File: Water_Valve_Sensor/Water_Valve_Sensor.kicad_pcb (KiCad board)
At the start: 2 copper layers, 73.5 x 30 mm, 30 parts, among them J1 Barrel_Jack, J2 WATER_PROBE, J3 SENSITIVITY_SELECTOR, J5 VALVE, Q1 Q_PMOS_DGS, U1 NE555D, U2 LM2904, U3 47U

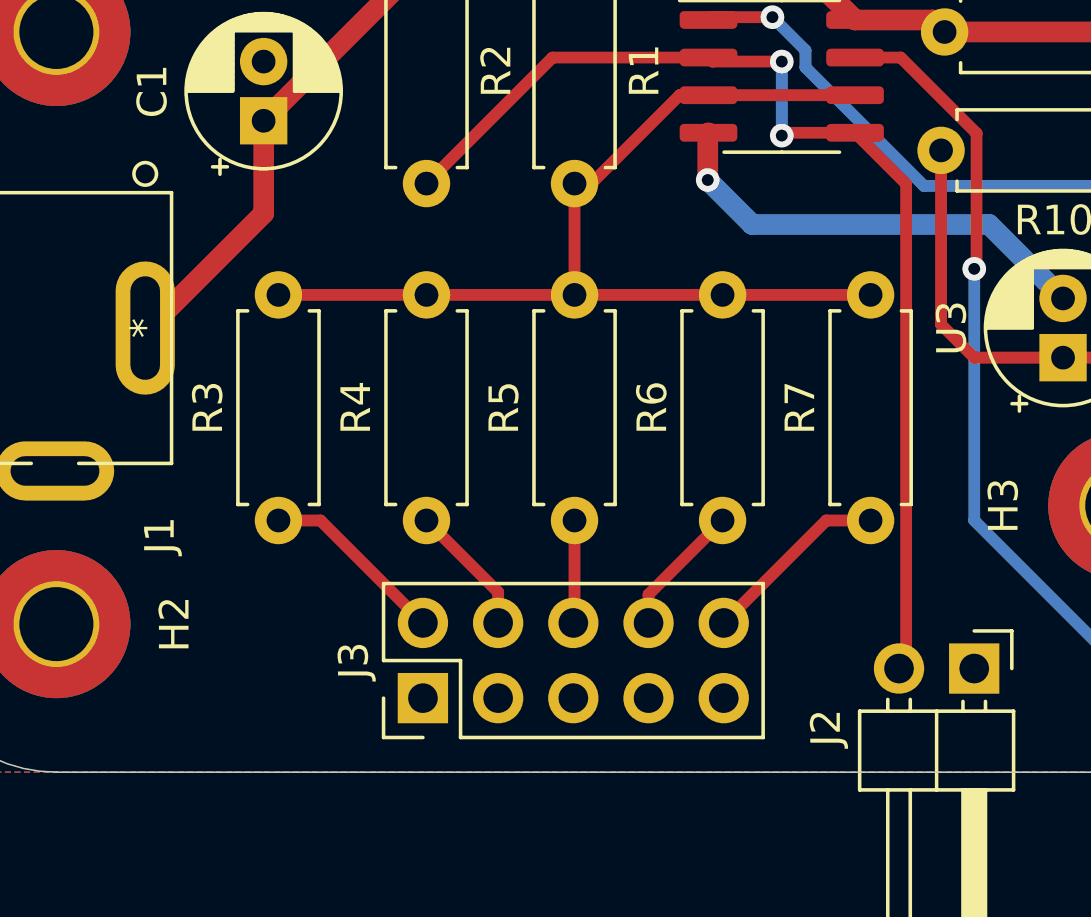
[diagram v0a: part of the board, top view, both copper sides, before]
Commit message: Fixed Wiring Issue
Added support for 2x6 header for Custom Setting Attachment
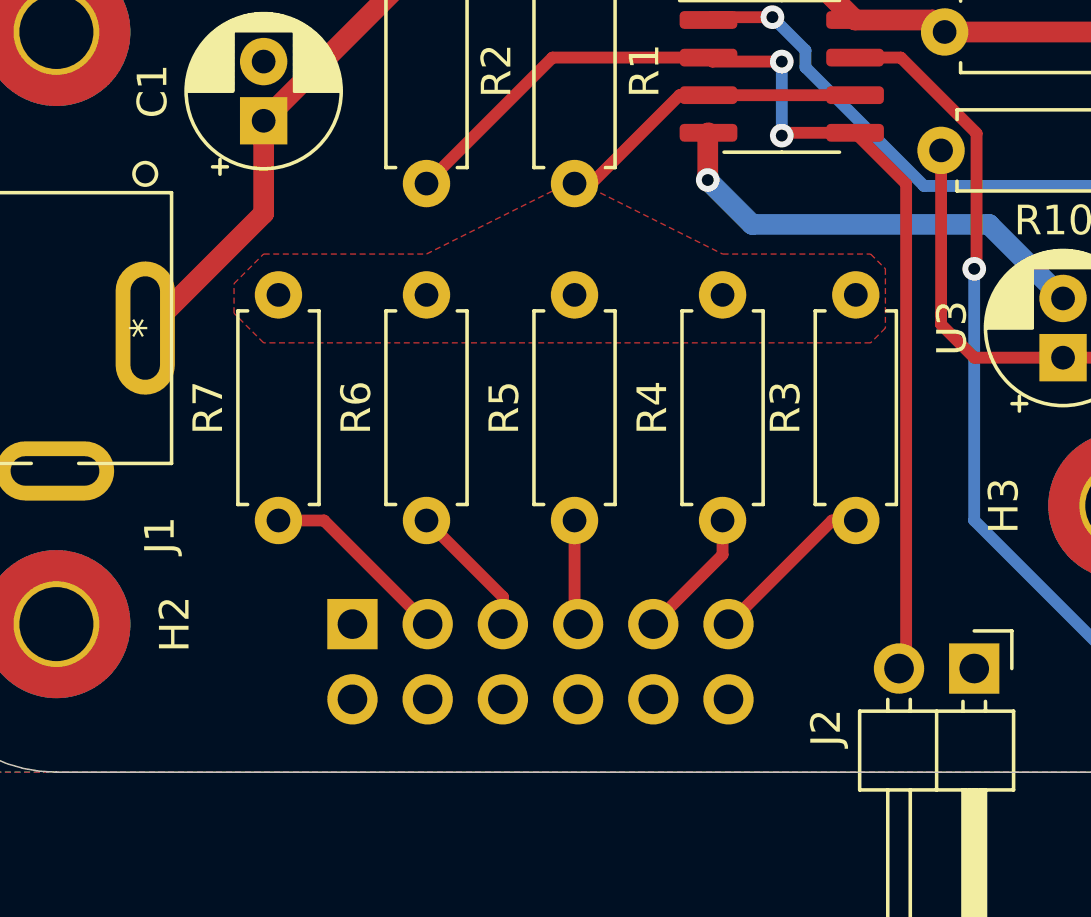
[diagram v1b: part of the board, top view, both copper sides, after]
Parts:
- J3: footprint Connector_PinHeader_2.54mm:PinHeader_2x05_P2.54mm_Vertical -> Connector_PinHeader_2.54mm:PinHeader_2x06_P2.54mm_Vertical; moved to B.Cu
- moved R7 20.0 mm to (47.5, 142.5)
- moved R3 19.5 mm to (67.0, 142.5)
- moved R4 10.0 mm to (62.5, 142.5)
- moved R6 10.0 mm to (52.5, 142.5)
- moved J3 3.45 mm to (50.0, 146.0), turned to 270 degrees
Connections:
- J3 pad 1: GND -> +12V
- J3 pad 10: Net-(J3-Pad10) -> GND
- J3 pad 2: Net-(J3-Pad2) -> +12V
- J3 pad 3: GND -> Net-(J3-Pad3)
- J3 pad 4: Net-(J3-Pad4) -> GND
- J3 pad 5: GND -> Net-(J3-Pad5)
- J3 pad 6: Net-(J3-Pad6) -> GND
- J3 pad 7: GND -> Net-(J3-Pad7)
- J3 pad 8: Net-(J3-Pad8) -> GND
- J3 pad 9: GND -> Net-(J3-Pad9)
- R3 pad 1: Net-(J3-Pad2) -> Net-(J3-Pad11)
- R4 pad 1: Net-(J3-Pad4) -> Net-(J3-Pad9)
- R5 pad 1: Net-(J3-Pad6) -> Net-(J3-Pad7)
- R6 pad 1: Net-(J3-Pad8) -> Net-(J3-Pad5)
- R7 pad 1: Net-(J3-Pad10) -> Net-(J3-Pad3)
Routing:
- net R_SENSITIVITY: track 34.5 -> 10.7 mm
- net Net-(J3-Pad3): track 0.00 -> 6.49 mm
- net Net-(J3-Pad10): track 6.39 -> 0.00 mm
- net Net-(J3-Pad2): track 6.31 -> 0.00 mm
- net Net-(J3-Pad11): track 0.00 -> 5.75 mm
- net Net-(J3-Pad5): track 0.00 -> 4.57 mm
- net Net-(J3-Pad8): track 4.50 -> 0.00 mm
- net Net-(J3-Pad9): track 0.00 -> 4.47 mm
- net Net-(J3-Pad4): track 4.46 -> 0.00 mm
- net Net-(J3-Pad7): track 0.00 -> 3.61 mm
- net Net-(J3-Pad6): track 3.48 -> 0.00 mm
- added copper zone on F.Cu, net R_SENSITIVITY

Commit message: Updated Resistor Combination
Updated Resistor Combination
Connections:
- J1 pad 3: (no net) -> GND
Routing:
- net +12V: track 85.1 -> 101.5 mm
- net GND: track 15.3 -> 13.7 mm
- net R_SENSITIVITY: track 10.7 -> 11.4 mm
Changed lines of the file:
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@@
     (thickness 1.6)
     (drawings 14)
-    (tracks 118)
+    (tracks 122)
     (zones 0)
     (modules 30)
@@
   )
   (setup
-    (last_trace_width 0.4)
+    (last_trace_width 0.7)
     (user_trace_width 0.4)
     (user_trace_width 0.7)
@@
     (pad 1 thru_hole oval (at 0 0 270) (size 4.5 2) (drill oval 3.5 1) (layers *.Cu *.Mask)
       (net 2 +12V))
-    (pad 3 thru_hole oval (at 4.826 3.048) (size 4 2) (drill oval 3 1) (layers *.Cu *.Mask))
+    (pad 3 thru_hole oval (at 4.826 3.048) (size 4 2) (drill oval 3 1) (layers *.Cu *.Mask)
+      (net 1 GND))
     (pad 2 thru_hole oval (at 0 6.096 270) (size 4 2) (drill oval 3 1) (layers *.Cu *.Mask)
       (net 1 GND))
@@
   (gr_line (start 35 126) (end 35 146) (layer Edge.Cuts) (width 0.05))
   (via (at 62 131) (size 0.8) (drill 0.4) (layers F.Cu B.Cu) (net 1))
-  (segment (start 62 129.43) (end 62.025 129.405) (width 0.7) (layer F.Cu) (net 1))
-  (segment (start 62 131) (end 62 129.43) (width 0.7) (layer F.Cu) (net 1))
   (segment (start 63.5 132.5) (end 62 131) (width 0.7) (layer B.Cu) (net 1))
   (segment (start 71.5 132.5) (end 63.5 132.5) (width 0.7) (layer B.Cu) (net 1))
@@
   (segment (start 94.5 140.5) (end 90 136) (width 0.7) (layer F.Cu) (net 2))
   (segment (start 94.5 141.5) (end 94.5 140.5) (width 0.7) (layer F.Cu) (net 2))
+  (segment (start 50 146) (end 50 148.54) (width 0.7) (layer F.Cu) (net 2))
+  (segment (start 43 140.55) (end 43 136) (width 0.7) (layer F.Cu) (net 2))
+  (segment (start 48.45 146) (end 43 140.55) (width 0.7) (layer F.Cu) (net 2))
+  (segment (start 50 146) (end 48.45 146) (width 0.7) (layer F.Cu) (net 2))
   (segment (start 93.38 148) (end 94.5 149.12) (width 0.4) (layer F.Cu) (net 3))
   (segment (start 90.54 148) (end 93.38 148) (width 0.4) (layer F.Cu) (net 3))
@@
   (segment (start 97.5 135.3) (end 84.2 135.3) (width 0.4) (layer B.Cu) (net 8))
   (segment (start 100.5 138.3) (end 97.5 135.3) (width 0.4) (layer B.Cu) (net 8))
-  (segment (start 58.065 131.12) (end 57.5 131.12) (width 0.4) (layer F.Cu) (net 9))
-  (segment (start 61.05 128.135) (end 58.065 131.12) (width 0.4) (layer F.Cu) (net 9))
+  (segment (start 66.975 128.135) (end 62.025 128.135) (width 0.4) (layer F.Cu) (net 9))
+  (segment (start 57.5 130) (end 57.5 131.12) (width 0.4) (layer F.Cu) (net 9))
+  (segment (start 59 128.5) (end 57.5 130) (width 0.4) (layer F.Cu) (net 9))
+  (segment (start 60.685 128.5) (end 59 128.5) (width 0.4) (layer F.Cu) (net 9))
+  (segment (start 61.05 128.135) (end 60.685 128.5) (width 0.4) (layer F.Cu) (net 9))
   (segment (start 62.025 128.135) (end 61.05 128.135) (width 0.4) (layer F.Cu) (net 9))
-  (segment (start 66.975 128.135) (end 62.025 128.135) (width 0.4) (layer F.Cu) (net 9))
   (segment (start 57.5 145.92) (end 57.46 145.96) (width 0.4) (layer F.Cu) (net 17))
   (segment (start 78.299999 130.799999) (end 77.5 130) (width 0.4) (layer F.Cu) (net 10))
@@
         (xy 62.5 133.5) (xy 67.5 133.5) (xy 68 134) (xy 68 136) (xy 67.5 136.5)
         (xy 47 136.5) (xy 46 135.5) (xy 46 134.5) (xy 47 133.5) (xy 52.5 133.5)
-        (xy 57.5 131)
+        (xy 57.5 129.5)
       )
     )

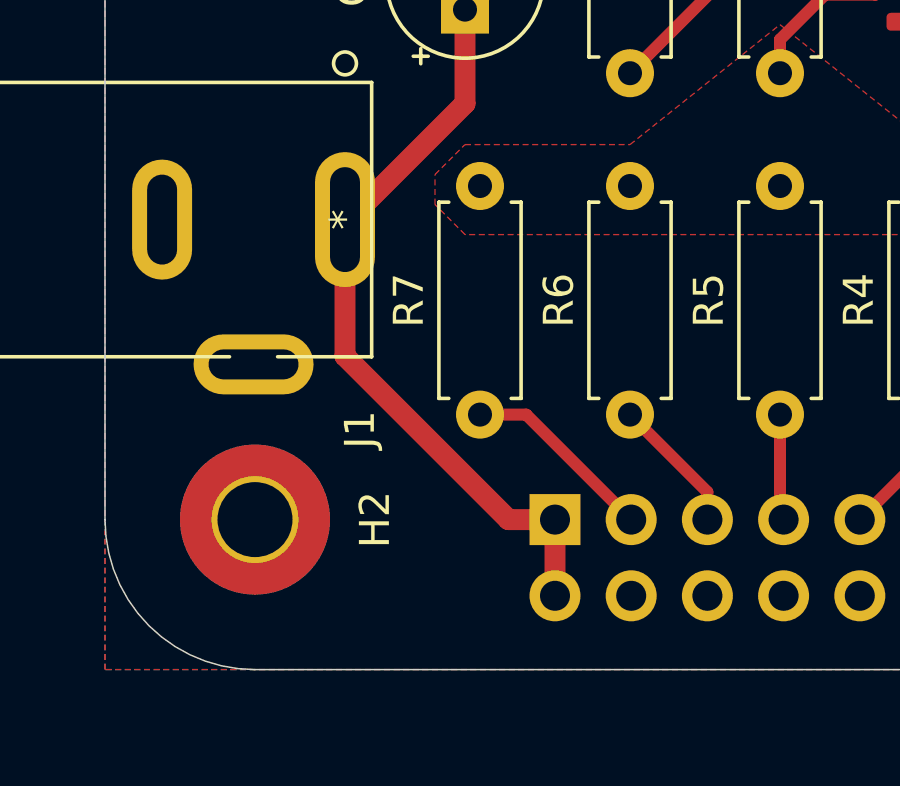
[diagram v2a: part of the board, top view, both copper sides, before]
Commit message: Changes to resistor selections
Updated sensitivty resistors.
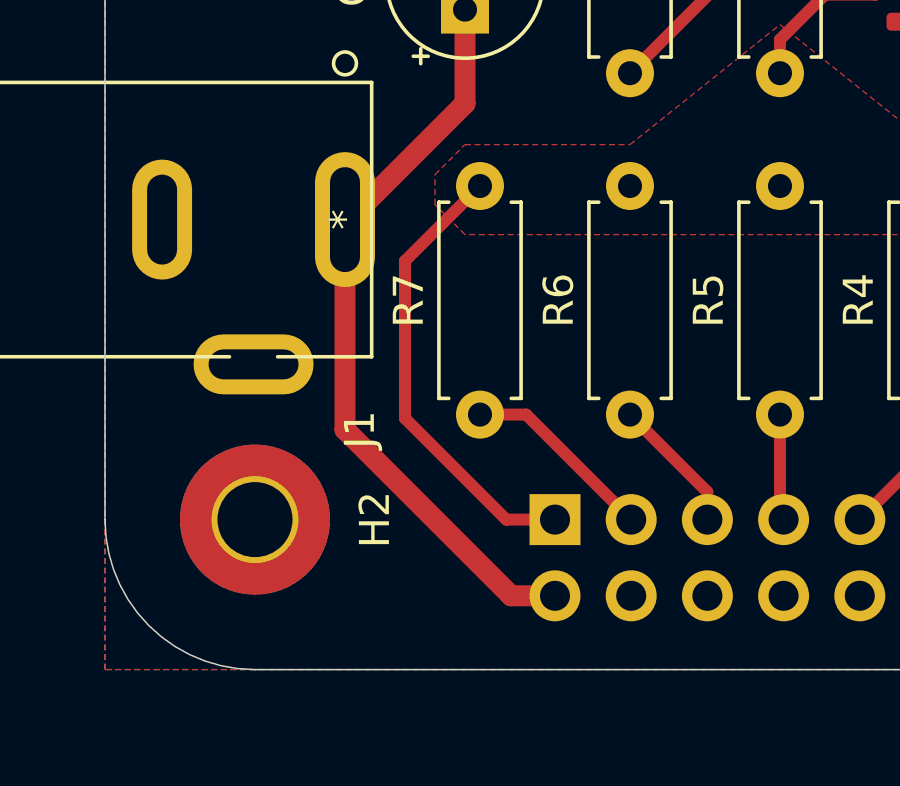
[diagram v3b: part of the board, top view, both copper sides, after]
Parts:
- R3: value 9K -> 383K
- R4: value 1K8 -> 255K
- R5: value 900R -> 127K
- R6: value 180R -> 63K4
- R7: value 91R -> 31K6
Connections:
- J3 pad 1: +12V -> R_SENSITIVITY
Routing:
- net R_SENSITIVITY: track 11.4 -> 26.5 mm
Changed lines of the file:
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@@
     (thickness 1.6)
     (drawings 14)
-    (tracks 122)
+    (tracks 125)
     (zones 0)
     (modules 30)
@@
   )
   (setup
-    (last_trace_width 0.7)
+    (last_trace_width 0.4)
     (user_trace_width 0.4)
     (user_trace_width 0.7)
@@
       (effects (font (size 1 1) (thickness 0.15)) (justify mirror))
     )
-    (fp_text user %R (at 1.27 -6.35) (layer B.Fab)
-      (effects (font (size 1 1) (thickness 0.15)) (justify mirror))
-    )
     (fp_line (start 0 1.27) (end 3.81 1.27) (layer B.Fab) (width 0.1))
     (fp_line (start 3.81 1.27) (end 3.81 -13.97) (layer B.Fab) (width 0.1))
@@
     (fp_line (start 4.35 -14.5) (end 4.35 1.8) (layer B.CrtYd) (width 0.05))
     (fp_line (start 4.35 1.8) (end -1.8 1.8) (layer B.CrtYd) (width 0.05))
+    (fp_text user %R (at 1.27 -6.35) (layer B.Fab)
+      (effects (font (size 1 1) (thickness 0.15)) (justify mirror))
+    )
     (pad 12 thru_hole oval (at 2.54 -12.7 270) (size 1.7 1.7) (drill 1) (layers *.Cu *.Mask)
       (net 1 GND))
@@
       (net 2 +12V))
     (pad 1 thru_hole rect (at 0 0 270) (size 1.7 1.7) (drill 1) (layers *.Cu *.Mask)
-      (net 2 +12V))
+      (net 9 R_SENSITIVITY))
     (model ${KISYS3DMOD}/Connector_PinHeader_2.54mm.3dshapes/PinHeader_2x06_P2.54mm_Vertical.wrl
       (at (xyz 0 0 0))
@@
       (effects (font (size 1 1) (thickness 0.15)))
     )
-    (fp_text value 91R (at 3.81 2.37 90) (layer F.Fab)
+    (fp_text value 31K6 (at 3.81 2.37 90) (layer F.Fab)
       (effects (font (size 1 1) (thickness 0.15)))
     )
@@
       (effects (font (size 1 1) (thickness 0.15)))
     )
-    (fp_text value 180R (at 3.81 2.37 90) (layer F.Fab)
+    (fp_text value 63K4 (at 3.81 2.37 90) (layer F.Fab)
       (effects (font (size 1 1) (thickness 0.15)))
     )
@@
       (effects (font (size 1 1) (thickness 0.15)))
     )
-    (fp_text value 900R (at 3.81 2.37 90) (layer F.Fab)
+    (fp_text value 127K (at 3.81 2.37 90) (layer F.Fab)
       (effects (font (size 1 1) (thickness 0.15)))
     )
@@
       (effects (font (size 1 1) (thickness 0.15)))
     )
-    (fp_text value 1K8 (at 3.81 2.37 90) (layer F.Fab)
+    (fp_text value 255K (at 3.81 2.37 90) (layer F.Fab)
       (effects (font (size 1 1) (thickness 0.15)))
     )
@@
       (effects (font (size 1 1) (thickness 0.15)))
     )
-    (fp_text value 9K (at 3.81 2.37 90) (layer F.Fab)
+    (fp_text value 383K (at 3.81 2.37 90) (layer F.Fab)
       (effects (font (size 1 1) (thickness 0.15)))
     )
@@
   (segment (start 94.5 140.5) (end 90 136) (width 0.7) (layer F.Cu) (net 2))
   (segment (start 94.5 141.5) (end 94.5 140.5) (width 0.7) (layer F.Cu) (net 2))
-  (segment (start 50 146) (end 50 148.54) (width 0.7) (layer F.Cu) (net 2))
-  (segment (start 43 140.55) (end 43 136) (width 0.7) (layer F.Cu) (net 2))
-  (segment (start 48.45 146) (end 43 140.55) (width 0.7) (layer F.Cu) (net 2))
-  (segment (start 50 146) (end 48.45 146) (width 0.7) (layer F.Cu) (net 2))
+  (segment (start 48.54 148.54) (end 50 148.54) (width 0.7) (layer F.Cu) (net 2))
+  (segment (start 43 143) (end 48.54 148.54) (width 0.7) (layer F.Cu) (net 2))
+  (segment (start 43 136) (end 43 143) (width 0.7) (layer F.Cu) (net 2))
   (segment (start 93.38 148) (end 94.5 149.12) (width 0.4) (layer F.Cu) (net 3))
   (segment (start 90.54 148) (end 93.38 148) (width 0.4) (layer F.Cu) (net 3))
@@
   (segment (start 61.05 128.135) (end 60.685 128.5) (width 0.4) (layer F.Cu) (net 9))
   (segment (start 62.025 128.135) (end 61.05 128.135) (width 0.4) (layer F.Cu) (net 9))
-  (segment (start 57.5 145.92) (end 57.46 145.96) (width 0.4) (layer F.Cu) (net 17))
+  (segment (start 48.375 146) (end 50 146) (width 0.4) (layer F.Cu) (net 9))
+  (segment (start 45 142.625) (end 48.375 146) (width 0.4) (layer F.Cu) (net 9))
+  (segment (start 45 137.38) (end 45 142.625) (width 0.4) (layer F.Cu) (net 9))
+  (segment (start 47.5 134.88) (end 45 137.38) (width 0.4) (layer F.Cu) (net 9))
   (segment (start 78.299999 130.799999) (end 77.5 130) (width 0.4) (layer F.Cu) (net 10))
   (segment (start 80.005707 130.799999) (end 78.299999 130.799999) (width 0.4) (layer F.Cu) (net 10))
@@
   (segment (start 62.5 143.66) (end 62.5 142.5) (width 0.4) (layer F.Cu) (net 16))
   (segment (start 60.16 146) (end 62.5 143.66) (width 0.4) (layer F.Cu) (net 16))
+  (segment (start 57.5 145.92) (end 57.46 145.96) (width 0.4) (layer F.Cu) (net 17))
   (segment (start 57.5 145.88) (end 57.62 146) (width 0.4) (layer F.Cu) (net 17))
   (segment (start 57.5 142.5) (end 57.5 145.88) (width 0.4) (layer F.Cu) (net 17))
